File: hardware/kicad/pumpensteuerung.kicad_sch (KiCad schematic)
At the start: 0 parts

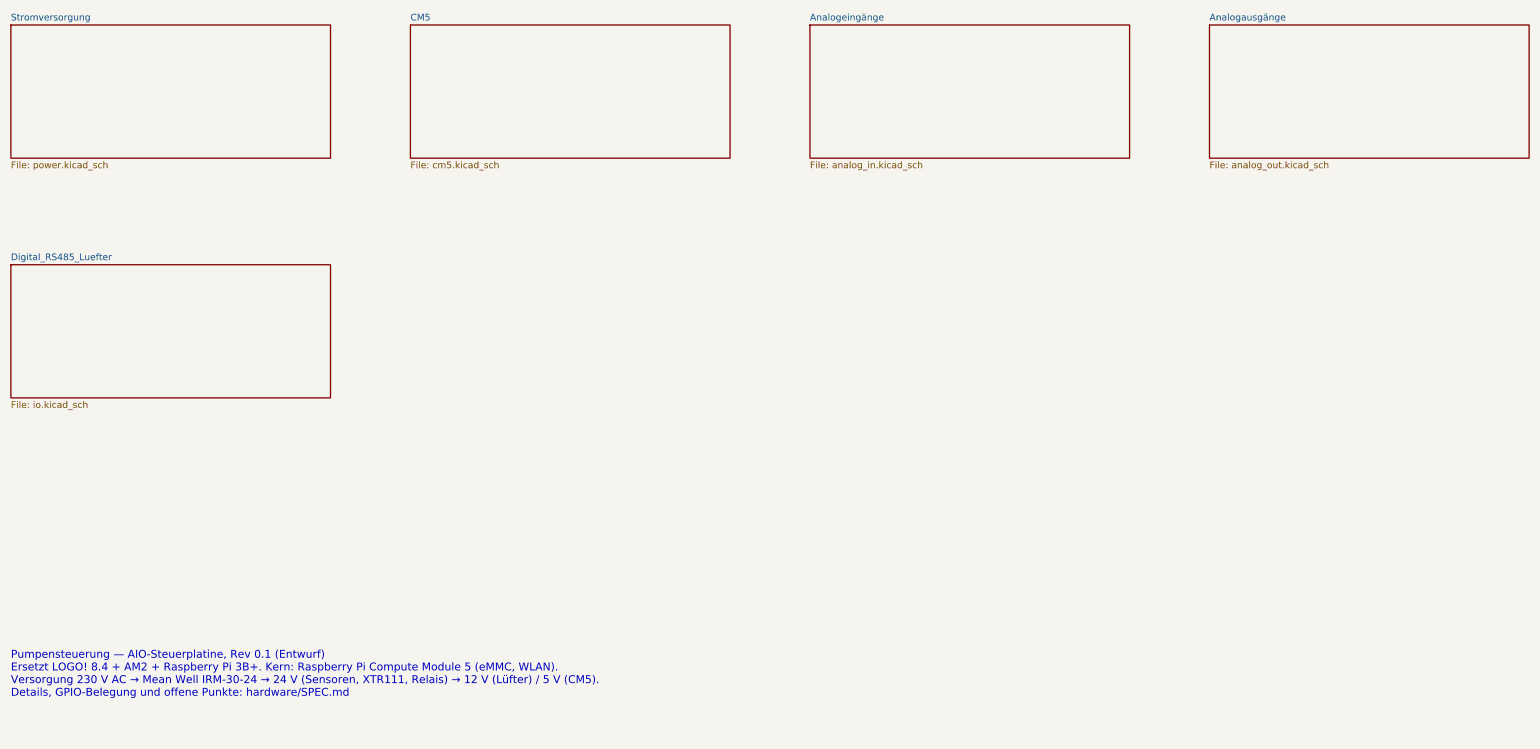
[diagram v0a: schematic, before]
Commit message: hardware: Rev 0.2 – ESP32-S3 (Steuerung) + M5Stack Stamp-P4 (App/HMI) statt CM5
CM5 entfernt. Neu: ESP32-S3-WROOM-1 für Regelung/I/O/V20, Stamp-P4 mit
LAN8720A-Ethernet und 7"-MIPI-DSI-Touch (FPC 15p), UART-Link mit Reset/Boot-
Steuerung des S3 durch den P4, 5V->3,3V-Wandler, USB-Werkbankversorgung.
I/O-Blätter unverändert. Netzliste geprüft (180 Netze, 0 Fehler).

Co-Authored-By: Claude Opus 5.5 <noreply@anthropic.com>
Claude-Session: https://claude.ai/code/session_019gH4tfEhDrFu8dTGZD88nH
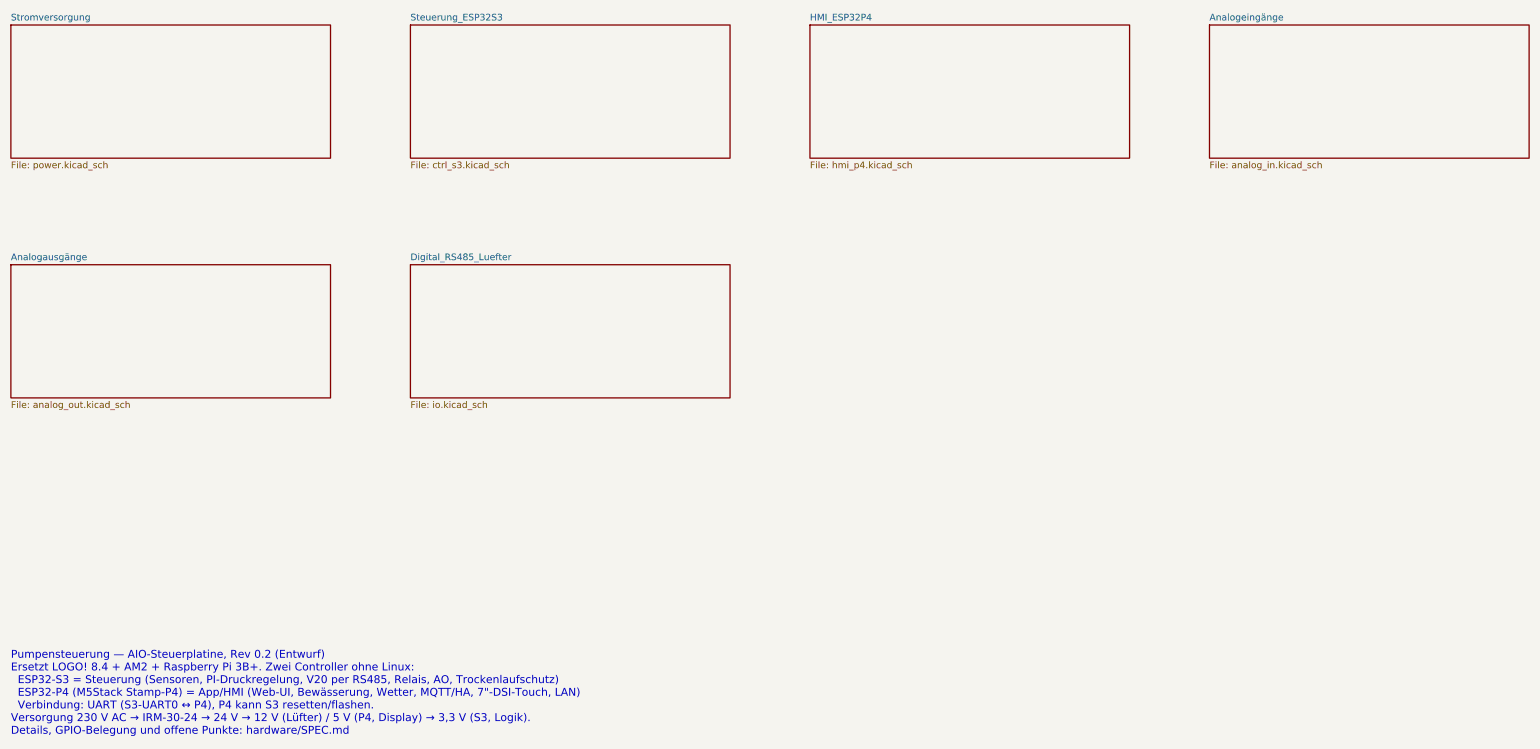
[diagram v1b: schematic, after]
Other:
- removed sheet CM5
- added sheet HMI_ESP32P4 (hmi_p4.kicad_sch)
- added sheet Steuerung_ESP32S3 (ctrl_s3.kicad_sch)
- note added: "Pumpensteuerung — AIO-Steuerplatine, Rev 0.2 (Entwurf) Ersetzt LOGO! 8.4 + AM2 + Raspberry Pi 3B+. Zwei Controller ohne Linux: ESP32-S3 = Steuerung (Sensoren, PI-Druckregelung, V20 per RS485, Relais, AO, Trockenlaufschutz) ESP32-P4 (M5Stack Stamp-P4) = App/HMI (Web-UI, Bewässerung, Wetter, MQTT/HA, 7"-DSI-Touch, LAN) Verbindung: UART (S3-UART0 ↔ P4), P4 kann S3 resetten/flashen. Versorgung 230 V 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"
- note removed: "Pumpensteuerung — AIO-Steuerplatine, Rev 0.1 (Entwurf) Ersetzt LOGO! 8.4 + AM2 + Raspberry Pi 3B+. Kern: Raspberry Pi Compute Module 5 (eMMC, WLAN). Versorgung 230 V AC → Mean Well IRM-30-24 → 24 V (Sensoren, XTR111, Relais) → 12 V (Lüfter) / 5 V (CM5). Details, GPIO-Belegung und offene Punkte: hardware/SPEC.md"
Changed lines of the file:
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@@
     (title "Pumpensteuerung — AIO-Steuerplatine (Übersicht)")
     (date "2026-10-20")
-    (rev "0.1")
+    (rev "0.2")
     (company "Brunnensteuerung Wathlingen")
     (comment 1 "Erzeugt mit hardware/tools/gen_schematic.py — Änderungen bitte dort"))
-  (text "Pumpensteuerung — AIO-Steuerplatine, Rev 0.1 (Entwurf)\nErsetzt LOGO! 8.4 + AM2 + Raspberry Pi 3B+. Kern: Raspberry Pi Compute Module 5 (eMMC, WLAN).\nVersorgung 230 V AC → Mean Well IRM-30-24 → 24 V (Sensoren, XTR111, Relais) → 12 V (Lüfter) / 5 V (CM5).\nDetails, GPIO-Belegung und offene Punkte: hardware/SPEC.md"
+  (text "Pumpensteuerung — AIO-Steuerplatine, Rev 0.2 (Entwurf)\nErsetzt LOGO! 8.4 + AM2 + Raspberry Pi 3B+. Zwei Controller ohne Linux:\n  ESP32-S3 = Steuerung (Sensoren, PI-Druckregelung, V20 per RS485, Relais, AO, Trockenlaufschutz)\n  ESP32-P4 (M5Stack Stamp-P4) = App/HMI (Web-UI, Bewässerung, Wetter, MQTT/HA, 7\"-DSI-Touch, LAN)\n  Verbindung: UART (S3-UART0 ↔ P4), P4 kann S3 resetten/flashen.\nVersorgung 230 V AC → IRM-30-24 → 24 V → 12 V (Lüfter) / 5 V (P4, Display) → 3,3 V (S3, Logik).\nDetails, GPIO-Belegung und offene Punkte: hardware/SPEC.md"
     (at 25.4 160 0)
     (effects
@@
     (instances
       (project "pumpensteuerung"
-        (path "/9e6f2443-112f-4320-930d-2fe5d449a19d"
+        (path "/549b275a-f11d-44a5-81ed-03dfc55c7e93"
           (page "2")))))
   (sheet
@@
     (fill
       (color 0 0 0 0))
-    (property "Sheetname" "CM5"
+    (property "Sheetname" "Steuerung_ESP32S3"
       (at 101.6 39.9284 0)
       (effects
@@
           (size 1.27 1.27))
         (justify left bottom)))
-    (property "Sheetfile" "cm5.kicad_sch"
+    (property "Sheetfile" "ctrl_s3.kicad_sch"
       (at 101.6 66.6246 0)
       (effects
@@
     (instances
       (project "pumpensteuerung"
-        (path "/9e6f2443-112f-4320-930d-2fe5d449a19d"
+        (path "/549b275a-f11d-44a5-81ed-03dfc55c7e93"
           (page "3")))))
   (sheet
@@
     (fill
       (color 0 0 0 0))
-    (property "Sheetname" "Analogeingänge"
+    (property "Sheetname" "HMI_ESP32P4"
       (at 177.8 39.9284 0)
       (effects
@@
           (size 1.27 1.27))
         (justify left bottom)))
-    (property "Sheetfile" "analog_in.kicad_sch"
+    (property "Sheetfile" "hmi_p4.kicad_sch"
       (at 177.8 66.6246 0)
       (effects
@@
     (instances
       (project "pumpensteuerung"
-        (path "/9e6f2443-112f-4320-930d-2fe5d449a19d"
+        (path "/549b275a-f11d-44a5-81ed-03dfc55c7e93"
           (page "4")))))
   (sheet
@@
     (fill
       (color 0 0 0 0))
-    (property "Sheetname" "Analogausgänge"
+    (property "Sheetname" "Analogeingänge"
       (at 254 39.9284 0)
       (effects
@@
           (size 1.27 1.27))
         (justify left bottom)))
-    (property "Sheetfile" "analog_out.kicad_sch"
+    (property "Sheetfile" "analog_in.kicad_sch"
       (at 254 66.6246 0)
       (effects
@@
     (instances
       (project "pumpensteuerung"
-        (path "/9e6f2443-112f-4320-930d-2fe5d449a19d"
+        (path "/549b275a-f11d-44a5-81ed-03dfc55c7e93"
           (page "5")))))
   (sheet
@@
     (fill
       (color 0 0 0 0))
-    (property "Sheetname" "Digital_RS485_Luefter"
+    (property "Sheetname" "Analogausgänge"
       (at 25.4 85.6484 0)
       (effects
@@
           (size 1.27 1.27))
         (justify left bottom)))
-    (property "Sheetfile" "io.kicad_sch"
+    (property "Sheetfile" "analog_out.kicad_sch"
       (at 25.4 112.3446 0)
       (effects
@@
     (instances
       (project "pumpensteuerung"
-        (path "/9e6f2443-112f-4320-930d-2fe5d449a19d"
+        (path "/549b275a-f11d-44a5-81ed-03dfc55c7e93"
           (page "6")))))
+  (sheet
+    (at 101.6 86.36)
+    (size 60.96 25.4)
+    (fields_autoplaced)
+    (stroke
+      (width 0.1524)
+      (type solid))
+    (fill
+      (color 0 0 0 0))
+    (property "Sheetname" "Digital_RS485_Luefter"
+      (at 101.6 85.6484 0)
+      (effects
+        (font
+          (size 1.27 1.27))
+        (justify left bottom)))
+    (property "Sheetfile" "io.kicad_sch"
+      (at 101.6 112.3446 0)
+      (effects
+        (font
+          (size 1.27 1.27))
+        (justify left top)))
+    (instances
+      (project "pumpensteuerung"
+        (path "/549b275a-f11d-44a5-81ed-03dfc55c7e93"
+          (page "7")))))
   (sheet_instances
     (path "/"

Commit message: hardware: Schaltplan im Block-Stil wie pool-pcb
Neuer Generator tools/schblock.py: gestrichelte Funktionsblöcke mit Titel und
Notizen, echte Drähte (eigener Router), Power-Symbole am Pin bzw. als Schiene,
Global-Labels nur an Blockgrenzen. Netzliste weiterhin gegen die deklarierte
Absicht geprüft (180 Netze, 0 Fehler), PWR_FLAGs ergänzt.

Co-Authored-By: Claude Opus 5.5 <noreply@anthropic.com>
Claude-Session: https://claude.ai/code/session_019gH4tfEhDrFu8dTGZD88nH
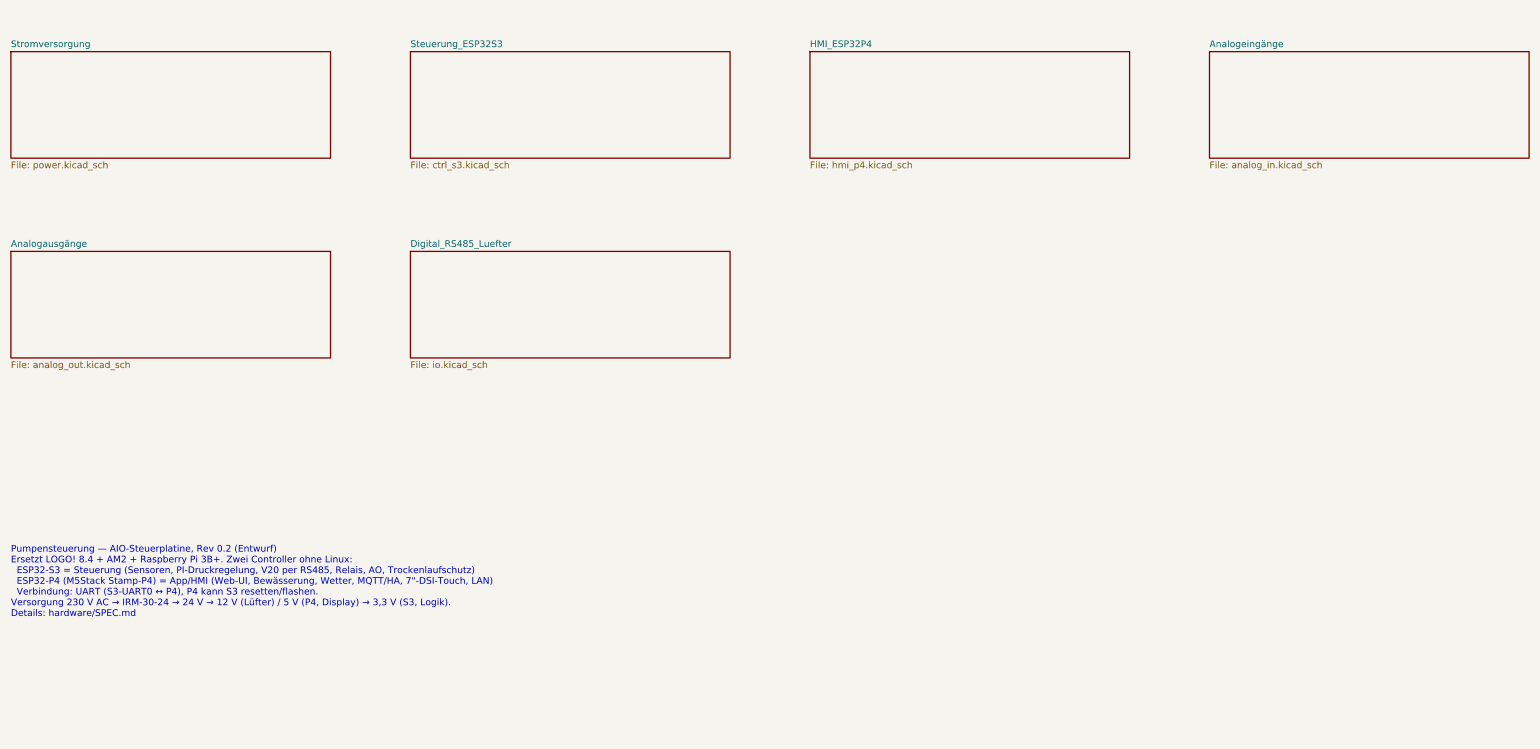
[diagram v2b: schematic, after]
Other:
- title: Pumpensteuerung — AIO-Steuerplatine (Übersicht) -> Pumpensteuerung — Übersicht
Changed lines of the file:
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@@
   (paper "A3")
   (title_block
-    (title "Pumpensteuerung — AIO-Steuerplatine (Übersicht)")
+    (title "Pumpensteuerung — Übersicht")
     (date "2026-10-20")
     (rev "0.2")
     (company "Brunnensteuerung Wathlingen")
-    (comment 1 "Erzeugt mit hardware/tools/gen_schematic.py — Änderungen bitte dort"))
-  (text "Pumpensteuerung — AIO-Steuerplatine, Rev 0.2 (Entwurf)\nErsetzt LOGO! 8.4 + AM2 + Raspberry Pi 3B+. Zwei Controller ohne Linux:\n  ESP32-S3 = Steuerung (Sensoren, PI-Druckregelung, V20 per RS485, Relais, AO, Trockenlaufschutz)\n  ESP32-P4 (M5Stack Stamp-P4) = App/HMI (Web-UI, Bewässerung, Wetter, MQTT/HA, 7\"-DSI-Touch, LAN)\n  Verbindung: UART (S3-UART0 ↔ P4), P4 kann S3 resetten/flashen.\nVersorgung 230 V AC → IRM-30-24 → 24 V → 12 V (Lüfter) / 5 V (P4, Display) → 3,3 V (S3, Logik).\nDetails, GPIO-Belegung und offene Punkte: hardware/SPEC.md"
-    (at 25.4 160 0)
+    (comment 1 "")
+    (comment 2 "Erzeugt mit hardware/tools/gen_schematic.py"))
+  (text "Pumpensteuerung — AIO-Steuerplatine, Rev 0.2 (Entwurf)\nErsetzt LOGO! 8.4 + AM2 + Raspberry Pi 3B+. Zwei Controller ohne Linux:\n  ESP32-S3 = Steuerung (Sensoren, PI-Druckregelung, V20 per RS485, Relais, AO, Trockenlaufschutz)\n  ESP32-P4 (M5Stack Stamp-P4) = App/HMI (Web-UI, Bewässerung, Wetter, MQTT/HA, 7\"-DSI-Touch, LAN)\n  Verbindung: UART (S3-UART0 ↔ P4), P4 kann S3 resetten/flashen.\nVersorgung 230 V AC → IRM-30-24 → 24 V → 12 V (Lüfter) / 5 V (P4, Display) → 3,3 V (S3, Logik).\nDetails: hardware/SPEC.md"
+    (at 25.4 140 0)
     (effects
       (font
-        (size 1.5 1.5))
+        (size 1.27 1.27))
       (justify left top))
 )
   (sheet
-    (at 25.4 40.64)
-    (size 60.96 25.4)
-    (fields_autoplaced)
+    (at 25.4 45.72)
+    (size 60.96 20.32)
     (stroke
       (width 0.1524)
@@
       (color 0 0 0 0))
     (property "Sheetname" "Stromversorgung"
-      (at 25.4 39.9284 0)
+      (at 25.4 45.0084 0)
       (effects
         (font
@@
     (instances
       (project "pumpensteuerung"
-        (path "/549b275a-f11d-44a5-81ed-03dfc55c7e93"
+        (path "/12fb2b20-dd6c-4acb-b1fb-fea61cd86825"
           (page "2")))))
   (sheet
-    (at 101.6 40.64)
-    (size 60.96 25.4)
-    (fields_autoplaced)
+    (at 101.6 45.72)
+    (size 60.96 20.32)
     (stroke
       (width 0.1524)
@@
       (color 0 0 0 0))
     (property "Sheetname" "Steuerung_ESP32S3"
-      (at 101.6 39.9284 0)
+      (at 101.6 45.0084 0)
       (effects
         (font
@@
     (instances
       (project "pumpensteuerung"
-        (path "/549b275a-f11d-44a5-81ed-03dfc55c7e93"
+        (path "/12fb2b20-dd6c-4acb-b1fb-fea61cd86825"
           (page "3")))))
   (sheet
-    (at 177.8 40.64)
-    (size 60.96 25.4)
-    (fields_autoplaced)
+    (at 177.8 45.72)
+    (size 60.96 20.32)
     (stroke
       (width 0.1524)
@@
       (color 0 0 0 0))
     (property "Sheetname" "HMI_ESP32P4"
-      (at 177.8 39.9284 0)
+      (at 177.8 45.0084 0)
       (effects
         (font
@@
     (instances
       (project "pumpensteuerung"
-        (path "/549b275a-f11d-44a5-81ed-03dfc55c7e93"
+        (path "/12fb2b20-dd6c-4acb-b1fb-fea61cd86825"
           (page "4")))))
   (sheet
-    (at 254 40.64)
-    (size 60.96 25.4)
-    (fields_autoplaced)
+    (at 254 45.72)
+    (size 60.96 20.32)
     (stroke
       (width 0.1524)
@@
       (color 0 0 0 0))
     (property "Sheetname" "Analogeingänge"
-      (at 254 39.9284 0)
+      (at 254 45.0084 0)
       (effects
         (font
@@
     (instances
       (project "pumpensteuerung"
-        (path "/549b275a-f11d-44a5-81ed-03dfc55c7e93"
+        (path "/12fb2b20-dd6c-4acb-b1fb-fea61cd86825"
           (page "5")))))
   (sheet
-    (at 25.4 86.36)
-    (size 60.96 25.4)
-    (fields_autoplaced)
+    (at 25.4 83.82)
+    (size 60.96 20.32)
     (stroke
       (width 0.1524)
@@
       (color 0 0 0 0))
     (property "Sheetname" "Analogausgänge"
-      (at 25.4 85.6484 0)
+      (at 25.4 83.1084 0)
       (effects
         (font
@@
         (justify left bottom)))
     (property "Sheetfile" "analog_out.kicad_sch"
-      (at 25.4 112.3446 0)
+      (at 25.4 104.7246 0)
       (effects
         (font
@@
     (instances
       (project "pumpensteuerung"
-        (path "/549b275a-f11d-44a5-81ed-03dfc55c7e93"
+        (path "/12fb2b20-dd6c-4acb-b1fb-fea61cd86825"
           (page "6")))))
   (sheet
-    (at 101.6 86.36)
-    (size 60.96 25.4)
-    (fields_autoplaced)
+    (at 101.6 83.82)
+    (size 60.96 20.32)
     (stroke
       (width 0.1524)
@@
       (color 0 0 0 0))
     (property "Sheetname" "Digital_RS485_Luefter"
-      (at 101.6 85.6484 0)
+      (at 101.6 83.1084 0)
       (effects
         (font
@@
         (justify left bottom)))
     (property "Sheetfile" "io.kicad_sch"
-      (at 101.6 112.3446 0)
+      (at 101.6 104.7246 0)
       (effects
         (font
@@
     (instances
       (project "pumpensteuerung"
-        (path "/549b275a-f11d-44a5-81ed-03dfc55c7e93"
+        (path "/12fb2b20-dd6c-4acb-b1fb-fea61cd86825"
           (page "7")))))
   (sheet_instances
